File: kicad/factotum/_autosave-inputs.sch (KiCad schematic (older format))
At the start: 33 parts, among them J4 Conn_01x10_Female, J5 VOCT, J6 Conn_01x10_Male, J7 SCL, J8 CLK, SW1 MODE_SW, U4 MCP6004, U5 ADC128S022

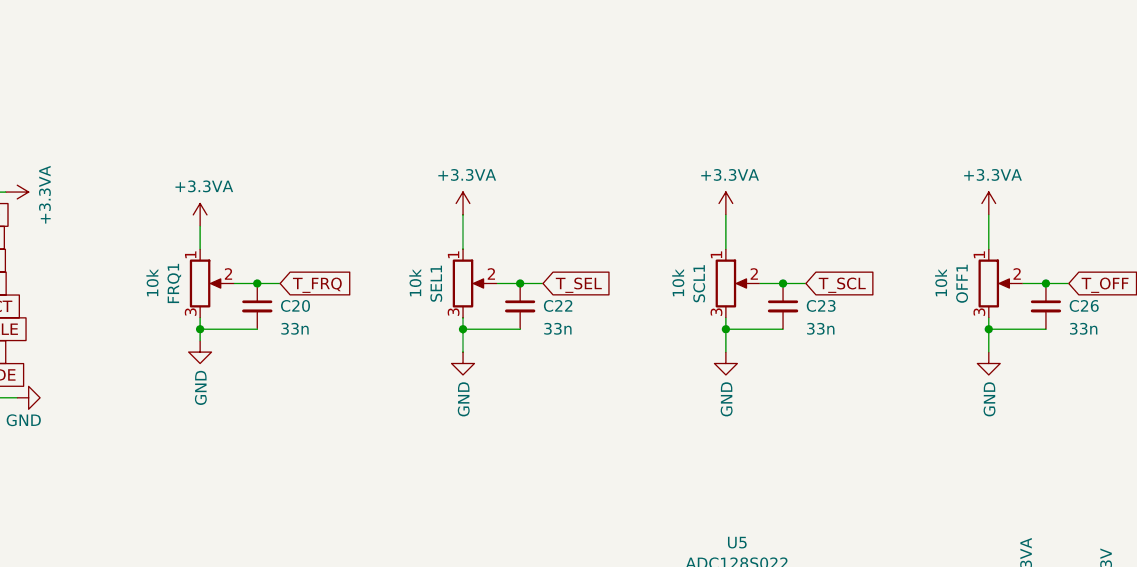
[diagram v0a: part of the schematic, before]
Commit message: initial layout of top board
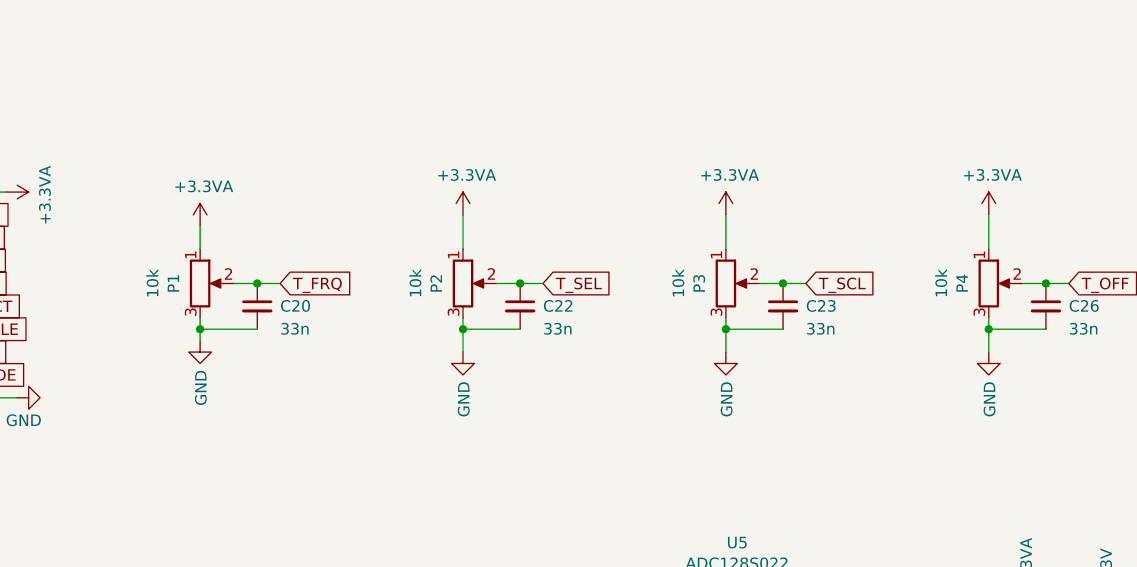
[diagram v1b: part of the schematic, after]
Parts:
- J5: footprint (none) -> Connector_Audio:Jack_3.5mm_QingPu_WQP-PJ398SM_Vertical_CircularHoles
- renumbered FRQ1 to P1, SEL1 to P2, SCL1 to P3, OFF1 to P4
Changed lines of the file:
@@
 F 0 "J5" H 1682 1975 50  0000 C CNN
 F 1 "VOCT" H 1682 1884 50  0000 C CNN
-F 2 "" H 1650 1650 50  0001 C CNN
+F 2 "Connector_Audio:Jack_3.5mm_QingPu_WQP-PJ398SM_Vertical_CircularHoles" H 1650 1650 50  0001 C CNN
 F 3 "~" H 1650 1650 50  0001 C CNN
 	1    1650 1650
@@
 P 3000 3400
 AR Path="/60807EF6" Ref="FRQ?"  Part="1"
-AR Path="/606FF2F2/60807EF6" Ref="FRQ1"  Part="1"
-F 0 "FRQ1" V 2885 3400 50  0000 C CNN
+AR Path="/606FF2F2/60807EF6" Ref="P1"  Part="1"
+F 0 "P1" V 2885 3400 50  0000 C CNN
 F 1 "10k" V 2794 3400 50  0000 C CNN
 F 2 "Potentiometer_THT:Potentiometer_Alpha_RD901F-40-00D_Single_Vertical_CircularHoles" H 3000 3400 50  0001 C CNN
@@
 P 4150 3400
 AR Path="/6082088B" Ref="FRQ?"  Part="1"
-AR Path="/606FF2F2/6082088B" Ref="SEL1"  Part="1"
-F 0 "SEL1" V 4035 3400 50  0000 C CNN
+AR Path="/606FF2F2/6082088B" Ref="P2"  Part="1"
+F 0 "P2" V 4035 3400 50  0000 C CNN
 F 1 "10k" V 3944 3400 50  0000 C CNN
 F 2 "Potentiometer_THT:Potentiometer_Alpha_RD901F-40-00D_Single_Vertical_CircularHoles" H 4150 3400 50  0001 C CNN
@@
 P 5300 3400
 AR Path="/6082982D" Ref="FRQ?"  Part="1"
-AR Path="/606FF2F2/6082982D" Ref="SCL1"  Part="1"
-F 0 "SCL1" V 5185 3400 50  0000 C CNN
+AR Path="/606FF2F2/6082982D" Ref="P3"  Part="1"
+F 0 "P3" V 5185 3400 50  0000 C CNN
 F 1 "10k" V 5094 3400 50  0000 C CNN
 F 2 "Potentiometer_THT:Potentiometer_Alpha_RD901F-40-00D_Single_Vertical_CircularHoles" H 5300 3400 50  0001 C CNN
@@
 P 6450 3400
 AR Path="/60829C62" Ref="FRQ?"  Part="1"
-AR Path="/606FF2F2/60829C62" Ref="OFF1"  Part="1"
-F 0 "OFF1" V 6335 3400 50  0000 C CNN
+AR Path="/606FF2F2/60829C62" Ref="P4"  Part="1"
+F 0 "P4" V 6335 3400 50  0000 C CNN
 F 1 "10k" V 6244 3400 50  0000 C CNN
 F 2 "Potentiometer_THT:Potentiometer_Alpha_RD901F-40-00D_Single_Vertical_CircularHoles" H 6450 3400 50  0001 C CNN
